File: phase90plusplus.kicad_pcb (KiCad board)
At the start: 2 copper layers, 40 parts, among them Q1 2N7000, Q2 2N7000, Q3 2N7000, Q4 2N7000, Q5 2N2219, U1 TL061, U2 TL061, U3 TL061, U4 TL061, U5 TL061, U6 TL061

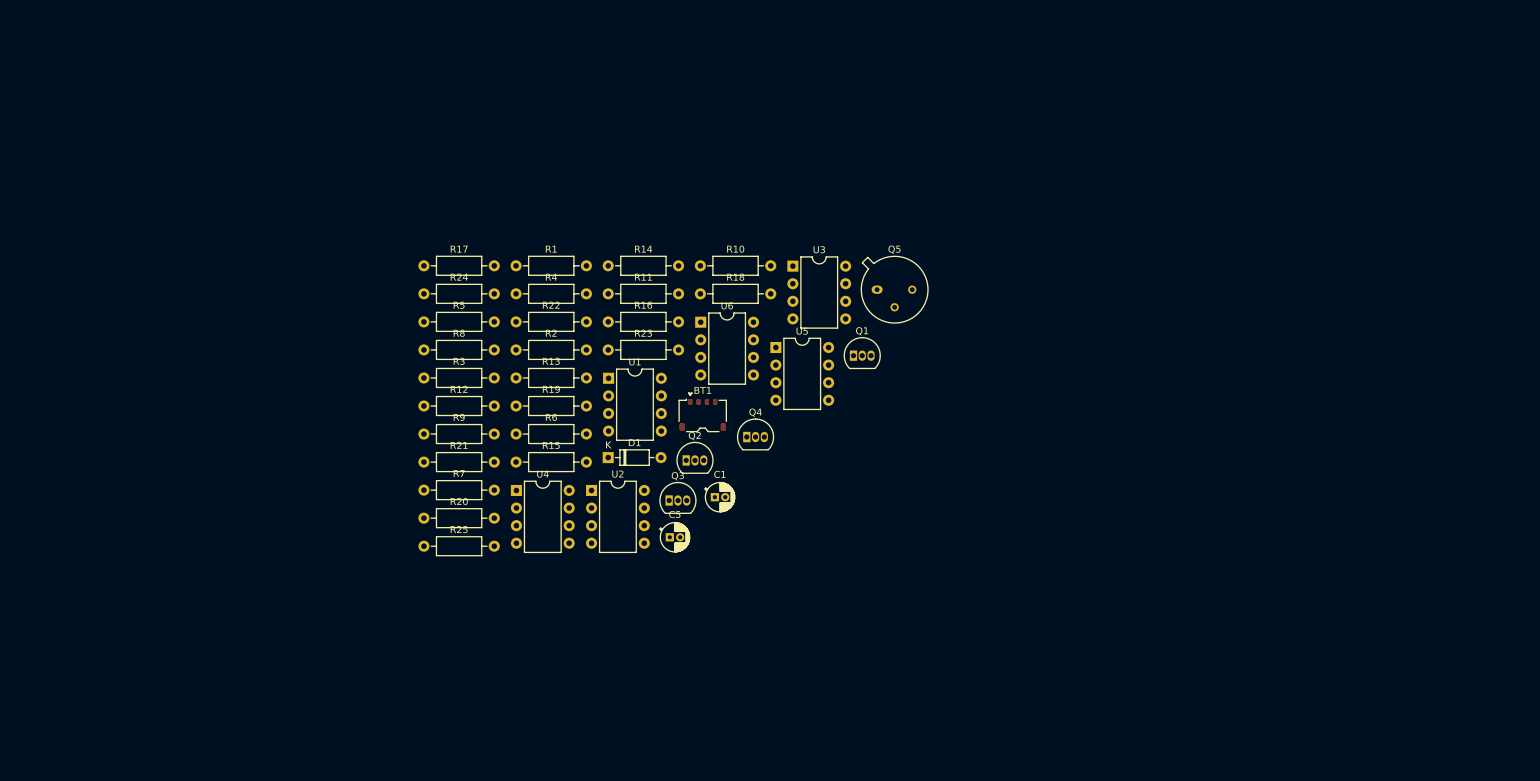
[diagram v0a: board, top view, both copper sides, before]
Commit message: Added libraries, initial routing and layout started.  Schematic revised to add LED and power handling.
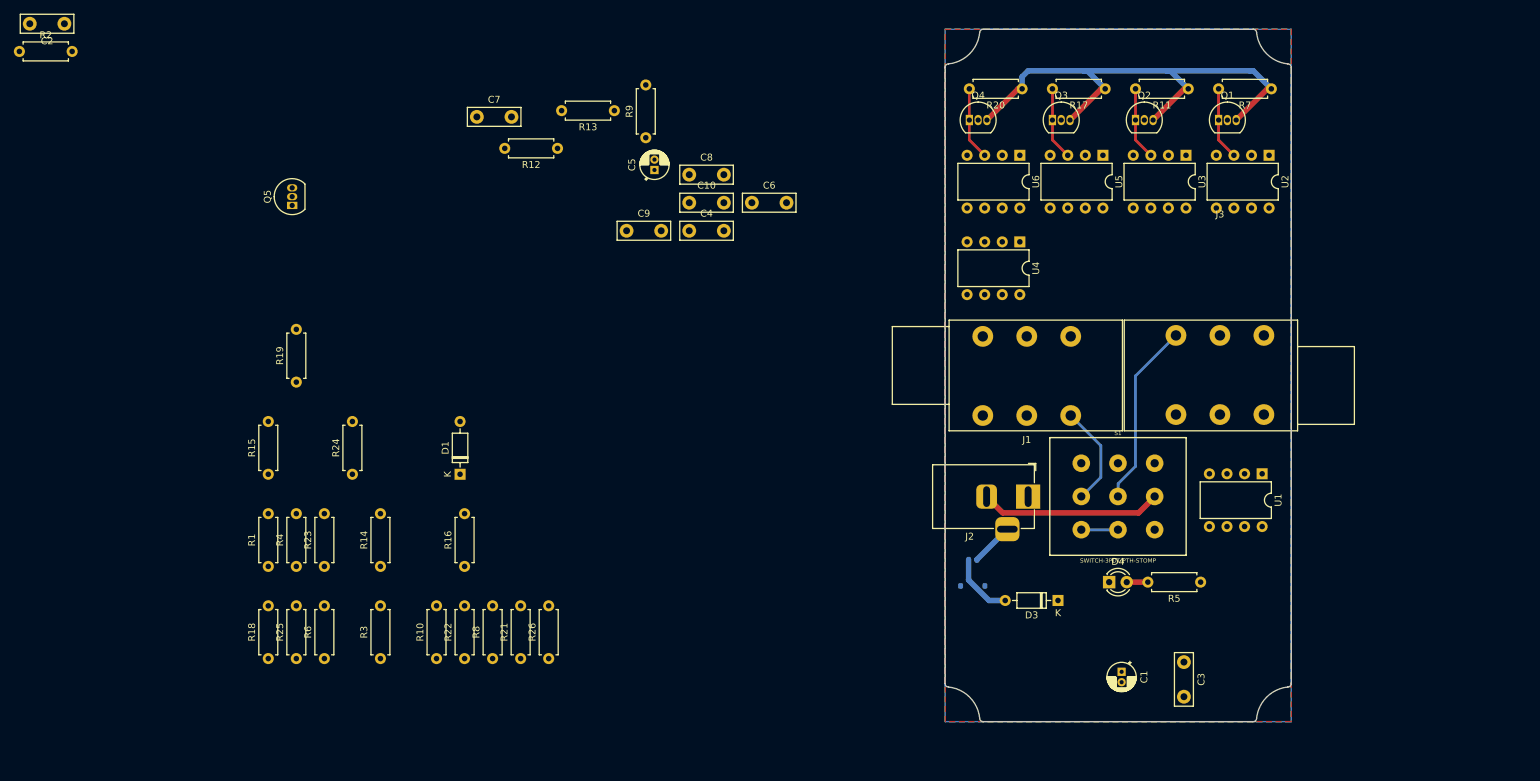
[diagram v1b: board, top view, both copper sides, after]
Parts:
- added C10: 47n, Capacitor_THT:C_Disc_D7.5mm_W2.5mm_P5.00mm, F.Cu at (148.1, 50.0)
- added C2: 0.01u, Capacitor_THT:C_Disc_D7.5mm_W2.5mm_P5.00mm, F.Cu at (57.8, 24.2)
- added C3: 47nF, Capacitor_THT:C_Disc_D7.5mm_W2.5mm_P5.00mm, F.Cu at (219.5, 116.4)
- added C4: 47n, Capacitor_THT:C_Disc_D7.5mm_W2.5mm_P5.00mm, F.Cu at (148.1, 54.1)
- added C6: 47n, Capacitor_THT:C_Disc_D7.5mm_W2.5mm_P5.00mm, F.Cu at (157.1, 50.0)
- added C7: 0.01u, Capacitor_THT:C_Disc_D7.5mm_W2.5mm_P5.00mm, F.Cu at (117.4, 37.6)
- added C8: 47n, Capacitor_THT:C_Disc_D7.5mm_W2.5mm_P5.00mm, F.Cu at (148.1, 46.0)
- added C9: 47n, Capacitor_THT:C_Disc_D7.5mm_W2.5mm_P5.00mm, F.Cu at (139.0, 54.1)
- added D3: 1N914, Diode_THT:D_DO-35_SOD27_P7.62mm_Horizontal, F.Cu at (201.3, 107.5)
- added D4: LED, LED_THT:LED_D3.0mm, F.Cu at (208.7, 104.8)
- added J1: AudioJack3, Connector_Audio:Jack_6.35mm_Neutrik_NRJ6HM-1_Horizontal, F.Cu at (203.2, 80.8)
- added J2: Barrel_Jack_Switch, Connector_BarrelJack:BarrelJack_Horizontal, F.Cu at (197.0, 92.5)
- added J3: AudioJack3, Connector_Audio:Jack_6.35mm_Neutrik_NRJ6HM-1_Horizontal, F.Cu at (218.3, 69.2)
- added R5: 370, Resistor_THT:R_Axial_DIN0207_L6.3mm_D2.5mm_P7.62mm_Horizontal, F.Cu at (221.9, 104.8)
- added S1: SWITCH-3PDT-PTH-STOMP, Switches:STOMP_SWITCH_3PDT, F.Cu at (210.0, 92.5)
- BT1: footprint Connector_JST:JST_ACH_BM04B-ACHSS-A-GAN-ETF_1x04-1MP_P1.20mm_Vertical -> Connector_JST:JST_ACH_BM02B-ACHSS-GAN-ETF_1x02-1MP_P1.20mm_Vertical; moved to B.Cu
- Q5: footprint Package_TO_SOT_THT:TO-39-3 -> Package_TO_SOT_THT:TO-92_Inline
- R1, R2, R3, R4: footprint Resistor_THT:R_Axial_DIN0207_L6.3mm_D2.5mm_P10.16mm_Horizontal -> Resistor_THT:R_Axial_DIN0207_L6.3mm_D2.5mm_P7.62mm_Horizontal
- R10: renamed from R9; footprint Resistor_THT:R_Axial_DIN0207_L6.3mm_D2.5mm_P10.16mm_Horizontal -> Resistor_THT:R_Axial_DIN0207_L6.3mm_D2.5mm_P7.62mm_Horizontal
- R11: renamed from R10; footprint Resistor_THT:R_Axial_DIN0207_L6.3mm_D2.5mm_P10.16mm_Horizontal -> Resistor_THT:R_Axial_DIN0207_L6.3mm_D2.5mm_P7.62mm_Horizontal
- R12: renamed from R11; footprint Resistor_THT:R_Axial_DIN0207_L6.3mm_D2.5mm_P10.16mm_Horizontal -> Resistor_THT:R_Axial_DIN0207_L6.3mm_D2.5mm_P7.62mm_Horizontal
- R13: renamed from R12; footprint Resistor_THT:R_Axial_DIN0207_L6.3mm_D2.5mm_P10.16mm_Horizontal -> Resistor_THT:R_Axial_DIN0207_L6.3mm_D2.5mm_P7.62mm_Horizontal
- R14: renamed from R13; footprint Resistor_THT:R_Axial_DIN0207_L6.3mm_D2.5mm_P10.16mm_Horizontal -> Resistor_THT:R_Axial_DIN0207_L6.3mm_D2.5mm_P7.62mm_Horizontal
- R15: renamed from R14; footprint Resistor_THT:R_Axial_DIN0207_L6.3mm_D2.5mm_P10.16mm_Horizontal -> Resistor_THT:R_Axial_DIN0207_L6.3mm_D2.5mm_P7.62mm_Horizontal
- R16: renamed from R15; footprint Resistor_THT:R_Axial_DIN0207_L6.3mm_D2.5mm_P10.16mm_Horizontal -> Resistor_THT:R_Axial_DIN0207_L6.3mm_D2.5mm_P7.62mm_Horizontal
- R17: renamed from R16; footprint Resistor_THT:R_Axial_DIN0207_L6.3mm_D2.5mm_P10.16mm_Horizontal -> Resistor_THT:R_Axial_DIN0207_L6.3mm_D2.5mm_P7.62mm_Horizontal
- R18: renamed from R17; footprint Resistor_THT:R_Axial_DIN0207_L6.3mm_D2.5mm_P10.16mm_Horizontal -> Resistor_THT:R_Axial_DIN0207_L6.3mm_D2.5mm_P7.62mm_Horizontal
- R19: renamed from R18; footprint Resistor_THT:R_Axial_DIN0207_L6.3mm_D2.5mm_P10.16mm_Horizontal -> Resistor_THT:R_Axial_DIN0207_L6.3mm_D2.5mm_P7.62mm_Horizontal
- R20: renamed from R19; footprint Resistor_THT:R_Axial_DIN0207_L6.3mm_D2.5mm_P10.16mm_Horizontal -> Resistor_THT:R_Axial_DIN0207_L6.3mm_D2.5mm_P7.62mm_Horizontal
- R21: renamed from R20; footprint Resistor_THT:R_Axial_DIN0207_L6.3mm_D2.5mm_P10.16mm_Horizontal -> Resistor_THT:R_Axial_DIN0207_L6.3mm_D2.5mm_P7.62mm_Horizontal
- R22: renamed from R21; footprint Resistor_THT:R_Axial_DIN0207_L6.3mm_D2.5mm_P10.16mm_Horizontal -> Resistor_THT:R_Axial_DIN0207_L6.3mm_D2.5mm_P7.62mm_Horizontal
- R23: renamed from R22; footprint Resistor_THT:R_Axial_DIN0207_L6.3mm_D2.5mm_P10.16mm_Horizontal -> Resistor_THT:R_Axial_DIN0207_L6.3mm_D2.5mm_P7.62mm_Horizontal
- R24: renamed from R23; footprint Resistor_THT:R_Axial_DIN0207_L6.3mm_D2.5mm_P10.16mm_Horizontal -> Resistor_THT:R_Axial_DIN0207_L6.3mm_D2.5mm_P7.62mm_Horizontal
- R25: renamed from R24; footprint Resistor_THT:R_Axial_DIN0207_L6.3mm_D2.5mm_P10.16mm_Horizontal -> Resistor_THT:R_Axial_DIN0207_L6.3mm_D2.5mm_P7.62mm_Horizontal
- R26: renamed from R25; footprint Resistor_THT:R_Axial_DIN0207_L6.3mm_D2.5mm_P10.16mm_Horizontal -> Resistor_THT:R_Axial_DIN0207_L6.3mm_D2.5mm_P7.62mm_Horizontal
- R6: renamed from R5; footprint Resistor_THT:R_Axial_DIN0207_L6.3mm_D2.5mm_P10.16mm_Horizontal -> Resistor_THT:R_Axial_DIN0207_L6.3mm_D2.5mm_P7.62mm_Horizontal
- R7: renamed from R6; footprint Resistor_THT:R_Axial_DIN0207_L6.3mm_D2.5mm_P10.16mm_Horizontal -> Resistor_THT:R_Axial_DIN0207_L6.3mm_D2.5mm_P7.62mm_Horizontal
- R8: renamed from R7; footprint Resistor_THT:R_Axial_DIN0207_L6.3mm_D2.5mm_P10.16mm_Horizontal -> Resistor_THT:R_Axial_DIN0207_L6.3mm_D2.5mm_P7.62mm_Horizontal
- R9: renamed from R8; footprint Resistor_THT:R_Axial_DIN0207_L6.3mm_D2.5mm_P10.16mm_Horizontal -> Resistor_THT:R_Axial_DIN0207_L6.3mm_D2.5mm_P7.62mm_Horizontal
- moved R7 119.9 mm to (232.1, 33.6), turned to 180 degrees
- moved U2 109.2 mm to (231.8, 43.2), turned to -90 degrees
- moved U1 95.4 mm to (230.8, 89.2), turned to -90 degrees
- moved R20 86.3 mm to (196.1, 33.6), turned to 180 degrees
- moved Q5 85.4 mm to (90.7, 50.4), turned to 90 degrees
- moved R2 83.7 mm to (51.3, 28.2)
- moved Q2 81.4 mm to (212.5, 38.1)
- moved U4 81.1 mm to (195.8, 55.7), turned to -90 degrees
- moved R17 79.3 mm to (208.1, 33.6), turned to 180 degrees
- moved Q3 78.0 mm to (200.5, 38.1)
- moved R11 75.0 mm to (220.1, 33.6), turned to 180 degrees
- moved C1 63.9 mm to (210.5, 117.8), turned to -90 degrees
- moved Q1 62.8 mm to (224.5, 38.1)
- moved R18 61.0 mm to (87.2, 115.9), turned to 90 degrees
- moved R19 59.7 mm to (91.3, 76.0), turned to 90 degrees
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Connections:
- BT1 pad 1: +9V -> Net-(BT1-Pad1)
- BT1 pad 2: GNDREF -> Net-(BT1-Pad2)
- R26 pad 2: /OUTPUT -> Net-(C10-Pad2)
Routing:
- net +5V: track 0.00 -> 75.4 mm
- net Net-(J3-PadT): track 0.00 -> 26.7 mm
- net Net-(J2-Pad2): track 0.00 -> 26.2 mm
- net Net-(J1-PadT): track 0.00 -> 15.3 mm
- net Net-(C9-Pad2): track 0.00 -> 10.5 mm
- net Net-(C8-Pad2): track 0.00 -> 10.5 mm
- net Net-(C6-Pad2): track 0.00 -> 10.5 mm
- net Net-(C4-Pad2): track 0.00 -> 10.5 mm
- net Net-(BT1-Pad2): track 0.00 -> 9.43 mm
- net Net-(BT1-Pad1): track 0.00 -> 6.25 mm
- net /OUTPUT: track 0.00 -> 5.30 mm
- net Net-(D4-Pad2): track 0.00 -> 3.05 mm
- added copper zone on B.Cu, net +9V
- added copper zone on F.Cu, net +9V
- added copper zone on B.Cu, net GNDREF
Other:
- board outline added: 50 x 100 mm

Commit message: Revision 1.0 complete.
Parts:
- removed D4: LED, LED_THT:LED_D3.0mm
- removed Q5: 2N2219, Package_TO_SOT_THT:TO-92_Inline
- removed U3, U4, U5, U6: TL061, Package_DIP:DIP-8_W7.62mm
- added C11: 100n, Capacitor_THT:C_Disc_D7.5mm_W2.5mm_P5.00mm, F.Cu at (250.5, 53.8)
- added C12: 100n, Capacitor_THT:C_Disc_D7.5mm_W2.5mm_P5.00mm, F.Cu at (255.5, 60.2)
- added D2: 1N914, Diode_THT:D_DO-35_SOD27_P7.62mm_Horizontal, F.Cu at (246.0, 73.0)
- added G***: LOGO, lib:art, B.Cu at (218.8, 79.2)
- added LFO1: STOMPLFO_DIP8, Package_DIP:DIP-8_W7.62mm_Socket, F.Cu at (237.5, 59.2)
- added RV1: 10k, Connector_Wire:SolderWire-0.1sqmm_1x03_P3.6mm_D0.4mm_OD1mm_Relief, F.Cu at (186.8, 57.8)
- added RV2: 10k, Connector_Wire:SolderWire-0.1sqmm_1x03_P3.6mm_D0.4mm_OD1mm_Relief, F.Cu at (252.4, 50.8)
- added RV3: 10k, Connector_Wire:SolderWire-0.1sqmm_1x03_P3.6mm_D0.4mm_OD1mm_Relief, F.Cu at (252.4, 40.6)
- BT1: footprint Connector_JST:JST_ACH_BM02B-ACHSS-GAN-ETF_1x02-1MP_P1.20mm_Vertical -> Connector_JST:JST_EH_S2B-EH_1x02_P2.50mm_Horizontal
- C1: value 15u -> 0.01u; footprint Capacitor_THT:CP_Radial_D4.0mm_P1.50mm -> Capacitor_THT:C_Disc_D7.5mm_W2.5mm_P5.00mm
- C10: value 47n -> 47nF
- C2, C7: value 0.01u -> 47n
- C3: value 47nF -> 47n
- C5: value 15u -> 47n; footprint Capacitor_THT:CP_Radial_D4.0mm_P1.50mm -> Capacitor_THT:C_Disc_D7.5mm_W2.5mm_P5.00mm
- C8: value 47n -> 4n7
- C9: value 47n -> 15u; footprint Capacitor_THT:C_Disc_D7.5mm_W2.5mm_P5.00mm -> Capacitor_THT:CP_Radial_D4.0mm_P1.50mm
- D1: value 1N914 -> LED; footprint Diode_THT:D_DO-35_SOD27_P7.62mm_Horizontal -> LED_THT:LED_D3.0mm
- D3: value 1N914 -> Zener
- J1: value AudioJack3 -> InputJack
- J2: value Barrel_Jack_Switch -> OutputJack; footprint Connector_BarrelJack:BarrelJack_Horizontal -> Connector_Audio:Jack_6.35mm_Neutrik_NRJ6HM-1_Horizontal
- J3: value AudioJack3 -> Barrel_Jack_Switch; footprint Connector_Audio:Jack_6.35mm_Neutrik_NRJ6HM-1_Horizontal -> Connector_BarrelJack:BarrelJack_Horizontal
- R1, R17, R21, R6, R8: footprint Resistor_THT:R_Axial_DIN0207_L6.3mm_D2.5mm_P7.62mm_Horizontal -> Resistor_THT:R_Axial_DIN0207_L6.3mm_D2.5mm_P10.16mm_Horizontal
- R10: value 10K -> 150K; footprint Resistor_THT:R_Axial_DIN0207_L6.3mm_D2.5mm_P7.62mm_Horizontal -> Resistor_THT:R_Axial_DIN0207_L6.3mm_D2.5mm_P10.16mm_Horizontal
- R11: value 24K -> 500k; footprint Resistor_THT:R_Axial_DIN0207_L6.3mm_D2.5mm_P7.62mm_Horizontal -> Resistor_THT:R_Axial_DIN0207_L6.3mm_D2.5mm_P10.16mm_Horizontal
- R12: value 150K -> 500; footprint Resistor_THT:R_Axial_DIN0207_L6.3mm_D2.5mm_P7.62mm_Horizontal -> Resistor_THT:R_Axial_DIN0207_L6.3mm_D2.5mm_P10.16mm_Horizontal
- R13: value 150K -> 500k; footprint Resistor_THT:R_Axial_DIN0207_L6.3mm_D2.5mm_P7.62mm_Horizontal -> Resistor_THT:R_Axial_DIN0207_L6.3mm_D2.5mm_P10.16mm_Horizontal
- R14, R16: value 10K -> 24K; footprint Resistor_THT:R_Axial_DIN0207_L6.3mm_D2.5mm_P7.62mm_Horizontal -> Resistor_THT:R_Axial_DIN0207_L6.3mm_D2.5mm_P10.16mm_Horizontal
- R15: value 470K -> 24K; footprint Resistor_THT:R_Axial_DIN0207_L6.3mm_D2.5mm_P7.62mm_Horizontal -> Resistor_THT:R_Axial_DIN0207_L6.3mm_D2.5mm_P10.16mm_Horizontal
- R18: value 10K -> 150k; footprint Resistor_THT:R_Axial_DIN0207_L6.3mm_D2.5mm_P7.62mm_Horizontal -> Resistor_THT:R_Axial_DIN0207_L6.3mm_D2.5mm_P10.16mm_Horizontal
- R19: value 10K -> 370; footprint Resistor_THT:R_Axial_DIN0207_L6.3mm_D2.5mm_P7.62mm_Horizontal -> Resistor_THT:R_Axial_DIN0207_L6.3mm_D2.5mm_P10.16mm_Horizontal
- R2, R3: value 500k -> 10K; footprint Resistor_THT:R_Axial_DIN0207_L6.3mm_D2.5mm_P7.62mm_Horizontal -> Resistor_THT:R_Axial_DIN0207_L6.3mm_D2.5mm_P10.16mm_Horizontal
- R20: value 24K -> 100K; footprint Resistor_THT:R_Axial_DIN0207_L6.3mm_D2.5mm_P7.62mm_Horizontal -> Resistor_THT:R_Axial_DIN0207_L6.3mm_D2.5mm_P10.16mm_Horizontal
- R22, R23, R24: value 150K -> 10K; footprint Resistor_THT:R_Axial_DIN0207_L6.3mm_D2.5mm_P7.62mm_Horizontal -> Resistor_THT:R_Axial_DIN0207_L6.3mm_D2.5mm_P10.16mm_Horizontal
- R25: value 56K -> 1K; footprint Resistor_THT:R_Axial_DIN0207_L6.3mm_D2.5mm_P7.62mm_Horizontal -> Resistor_THT:R_Axial_DIN0207_L6.3mm_D2.5mm_P10.16mm_Horizontal
- R26: value 150k -> 1K; footprint Resistor_THT:R_Axial_DIN0207_L6.3mm_D2.5mm_P7.62mm_Horizontal -> Resistor_THT:R_Axial_DIN0207_L6.3mm_D2.5mm_P10.16mm_Horizontal
- R4: value 1M -> 10K; footprint Resistor_THT:R_Axial_DIN0207_L6.3mm_D2.5mm_P7.62mm_Horizontal -> Resistor_THT:R_Axial_DIN0207_L6.3mm_D2.5mm_P10.16mm_Horizontal
- R5: value 370 -> 150K; footprint Resistor_THT:R_Axial_DIN0207_L6.3mm_D2.5mm_P7.62mm_Horizontal -> Resistor_THT:R_Axial_DIN0207_L6.3mm_D2.5mm_P10.16mm_Horizontal
- R7: value 24K -> 10K; footprint Resistor_THT:R_Axial_DIN0207_L6.3mm_D2.5mm_P7.62mm_Horizontal -> Resistor_THT:R_Axial_DIN0207_L6.3mm_D2.5mm_P10.16mm_Horizontal
- R9: value 3M9 -> 10K; footprint Resistor_THT:R_Axial_DIN0207_L6.3mm_D2.5mm_P7.62mm_Horizontal -> Resistor_THT:R_Axial_DIN0207_L6.3mm_D2.5mm_P10.16mm_Horizontal
- U1: value TL061 -> TL074; footprint Package_DIP:DIP-8_W7.62mm -> Package_DIP:DIP-14_W7.62mm
- U2: value TL061 -> TL072
- moved R25 167.5 mm to (248.1, 57.0), turned to 0 degrees
- moved R23 166.9 mm to (258.3, 66.6), turned to 180 degrees
- moved R4 156.0 mm to (229.9, 31.0), turned to 180 degrees
- moved R2 145.5 mm to (196.5, 37.2)
- moved R24 143.4 mm to (242.6, 83.1)
- moved C2 143.1 mm to (199.1, 46.8), turned to 0 degrees
- moved R3 141.0 mm to (229.9, 53.4), turned to 180 degrees
- moved R26 140.7 mm to (258.3, 63.4), turned to 180 degrees
- moved R22 130.5 mm to (234.4, 61.8), turned to 180 degrees
- moved R16 128.5 mm to (229.9, 43.8), turned to 180 degrees
- moved R8 128.3 mm to (229.9, 50.2), turned to 180 degrees
- moved R19 127.5 mm to (218.8, 80.7), turned to -90 degrees
- moved R15 123.9 mm to (196.5, 30.8), turned to 0 degrees
- moved C7 123.2 mm to (239.3, 55.2), turned to 180 degrees
- moved R21 121.9 mm to (234.5, 65.0), turned to 180 degrees
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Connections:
- BT1 pad 2: Net-(BT1-Pad2) -> /RING
- C1 pad 1: +5V -> Net-(C1-Pad1)
- C1 pad 2: GNDREF -> Net-(C1-Pad2)
- C10 pad 1: Net-(C10-Pad1) -> GNDREF
- C10 pad 2: Net-(C10-Pad2) -> +5V
- C2 pad 1: Net-(C2-Pad1) -> /U1_LOOPBACK
- C3 pad 1: VDD -> Net-(C3-Pad1)
- C3 pad 2: +5V -> Net-(C3-Pad2)
- C4 pad 1: /U1_LOOPBACK -> Net-(C4-Pad1)
- C5 pad 2: GNDREF -> Net-(C5-Pad2)
- C7 pad 1: Net-(C7-Pad1) -> GNDREF
- C7 pad 2: Net-(C7-Pad2) -> /LFO_OUT
- C8 pad 1: Net-(C8-Pad1) -> GNDREF
- C9 pad 1: Net-(C9-Pad1) -> +5V
- C9 pad 2: Net-(C9-Pad2) -> GNDREF
- D1 pad 1: +5V -> GNDREF
- D1 pad 2: GNDREF -> Net-(D1-Pad2)
- D3 pad 1: GNDREF -> +5V
- D3 pad 2: Net-(BT1-Pad2) -> GNDREF
- J1 pad RN: (no net) -> unconnected-(J1-PadRN)
- J1 pad SN: (no net) -> unconnected-(J1-PadSN)
- J1 pad TN: (no net) -> unconnected-(J1-PadTN)
- Q1 pad 1: Net-(C4-Pad2) -> /LFO_OUT
- Q1 pad 2: VDD -> Net-(C2-Pad2)
- Q2 pad 1: Net-(C6-Pad2) -> /LFO_OUT
- Q2 pad 2: VDD -> Net-(C3-Pad2)
- Q3 pad 1: Net-(C8-Pad2) -> /LFO_OUT
- Q3 pad 2: VDD -> Net-(C4-Pad2)
- Q4 pad 1: Net-(C9-Pad2) -> /LFO_OUT
- Q4 pad 2: VDD -> Net-(C5-Pad2)
- R1 pad 1: +9V -> Net-(R1-Pad1)
- R1 pad 2: +5V -> Net-(C3-Pad1)
- R10 pad 1: Net-(C6-Pad1) -> Net-(R10-Pad1)
- R11 pad 1: +5V -> Net-(R11-Pad1)
- R11 pad 2: Net-(C6-Pad2) -> Net-(C1-Pad1)
- R12 pad 1: Net-(C7-Pad1) -> Net-(R12-Pad1)
- R12 pad 2: Net-(C5-Pad1) -> Net-(C6-Pad2)
- R13 pad 1: Net-(R13-Pad1) -> +5V
- R13 pad 2: +5V -> Net-(C1-Pad2)
- R14 pad 1: Net-(R10-Pad2) -> +5V
- R14 pad 2: Net-(C8-Pad1) -> Net-(C2-Pad2)
- R15 pad 1: Net-(C7-Pad2) -> +5V
- R15 pad 2: Net-(R13-Pad1) -> Net-(C3-Pad2)
- R16 pad 1: Net-(C8-Pad1) -> +5V
- R16 pad 2: Net-(R16-Pad2) -> Net-(C4-Pad2)
- R17 pad 2: Net-(C8-Pad2) -> Net-(C5-Pad2)
- R18 pad 1: Net-(R16-Pad2) -> GNDREF
- R18 pad 2: Net-(C9-Pad1) -> Net-(C6-Pad2)
- R19 pad 1: Net-(C9-Pad1) -> +9V
- R19 pad 2: Net-(R19-Pad2) -> Net-(D1-Pad2)
- R2 pad 2: Net-(C2-Pad1) -> Net-(C4-Pad1)
- R20 pad 1: +5V -> Net-(C8-Pad2)
- R20 pad 2: Net-(C9-Pad2) -> /LFO_OUT
- R21 pad 1: Net-(R19-Pad2) -> /LFO
- R21 pad 2: Net-(R21-Pad2) -> Net-(C8-Pad2)
- R22 pad 1: Net-(R21-Pad2) -> Net-(LFO1-Pad2)
- R22 pad 2: Net-(Q5-Pad2) -> GNDREF
- R23 pad 1: /U1_LOOPBACK -> +5V
- R23 pad 2: Net-(Q5-Pad2) -> Net-(LFO1-Pad5)
- R24 pad 1: Net-(Q5-Pad2) -> +9V
- R24 pad 2: Net-(C10-Pad1) -> +5V
- R25 pad 1: GNDREF -> Net-(R25-Pad1)
- R25 pad 2: Net-(C10-Pad1) -> /FRQ
- R26 pad 1: GNDREF -> Net-(R26-Pad1)
- R26 pad 2: Net-(C10-Pad2) -> /WVF
- R3 pad 1: VAA -> Net-(R3-Pad1)
- R3 pad 2: Net-(C2-Pad2) -> Net-(C5-Pad1)
- R4 pad 2: VDD -> Net-(R10-Pad1)
- R5 pad 1: +9V -> Net-(R10-Pad2)
- R5 pad 2: Net-(D4-Pad2) -> Net-(C6-Pad1)
- R6 pad 2: Net-(R6-Pad2) -> Net-(R1-Pad1)
- R7 pad 1: +5V -> Net-(C3-Pad1)
- R7 pad 2: Net-(C4-Pad2) -> Net-(R2-Pad1)
- R8 pad 1: Net-(R6-Pad2) -> Net-(C4-Pad1)
- R8 pad 2: Net-(C6-Pad1) -> Net-(R3-Pad1)
- R9 pad 2: VDD -> Net-(R4-Pad1)
- S1 pad P$1: Net-(R2-Pad1) -> Net-(R11-Pad1)
- S1 pad P$2: Net-(J1-PadT) -> Net-(J1-PadT1)
- S1 pad P$4: Net-(C10-Pad2) -> Net-(R12-Pad1)
- S1 pad P$5: Net-(J3-PadT) -> Net-(J2-PadT1)
- S1 pad P$8: Net-(J2-Pad2) -> Net-(J3-Pad2)
- U1 pad 1: unconnected-(U1-Pad1) -> Net-(C4-Pad1)
- U1 pad 2: /U1_LOOPBACK -> Net-(R2-Pad1)
- U1 pad 3: Net-(C2-Pad2) -> Net-(C3-Pad2)
- U1 pad 4: GNDREF -> +9V
- U1 pad 5: unconnected-(U1-Pad5) -> Net-(C2-Pad2)
- U1 pad 6: /U1_LOOPBACK -> Net-(R1-Pad1)
- U1 pad 7: +9V -> Net-(C3-Pad1)
- U1 pad 8: unconnected-(U1-Pad8) -> Net-(C5-Pad1)
- U2 pad 1: unconnected-(U2-Pad1) -> Net-(C6-Pad1)
- U2 pad 2: Net-(R6-Pad2) -> Net-(R10-Pad2)
- U2 pad 3: Net-(C4-Pad2) -> +5V
- U2 pad 5: unconnected-(U2-Pad5) -> Net-(C1-Pad2)
- U2 pad 6: Net-(C6-Pad1) -> /U1_LOOPBACK
- U2 pad 7: +9V -> /U1_LOOPBACK
- U2 pad 8: unconnected-(U2-Pad8) -> +9V
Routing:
- net GNDREF: track 0.00 -> 327.4 mm, vias 0 -> 1
- net +5V: track 75.4 -> 230.9 mm, vias 0 -> 1
- net +9V: track 0.00 -> 107.3 mm
- net /LFO_OUT: track 0.00 -> 94.2 mm
- net Net-(J2-PadT1): track 0.00 -> 48.6 mm
- net Net-(J3-Pad2): track 0.00 -> 48.3 mm
- net /U1_LOOPBACK: track 0.00 -> 42.5 mm
- net Net-(R26-Pad1): track 0.00 -> 33.4 mm
- net Net-(C3-Pad1): track 0.00 -> 31.4 mm
- net Net-(R10-Pad2): track 0.00 -> 31.4 mm
- net Net-(C6-Pad2): track 10.5 -> 41.7 mm
- net Net-(C4-Pad1): track 0.00 -> 28.9 mm
- net Net-(C3-Pad2): track 0.00 -> 28.3 mm
- net Net-(R10-Pad1): track 0.00 -> 28.0 mm
- net Net-(J3-PadT): track 26.7 -> 0.00 mm
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- removed copper zone on B.Cu, net +9V
- removed copper zone on F.Cu, net +9V
- removed copper zone on B.Cu, net GNDREF
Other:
- board size 50 x 100 mm -> 84 x 105 mm
